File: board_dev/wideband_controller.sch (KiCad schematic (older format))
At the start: 55 parts, among them J1 Conn_02x05_Odd_Even, J2 Conn_01x06, J3 Conn_01x08, Q1 BTS3028, U1 MCP6004, U2 MCP6004, U4 STM32F042K6Ux, U9 XC6206P332MR

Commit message: cleanup & tweaks
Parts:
- R1: value 15k -> 10k; LCSC (none) -> C25744
- R5, R7: value 30k -> 27k; LCSC (none) -> C25711
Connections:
- net +3V3: now also U1.4 (V+); no longer U1.11 (V-)
- net GND: now also U1.11 (V-); no longer U1.4 (V+)
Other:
- note added: "Un_sense = 2.7 * (Un - Vm)"
- note removed: "Un_sense = 3 * (Un - Vm)"
- moved on the sheet: C10, C11, C12, C13, C14, C15, C7, C8, C9, D1, D2, J1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

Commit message: add note
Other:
- note added: "0.2v reference"
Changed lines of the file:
@@
 	1    0    0    -1
 $EndComp
+Text Notes 1175 5150 0    50   ~ 0
+0.2v reference
 $EndSCHEMATC

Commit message: layout help from dave
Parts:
- added C16: 1u, Capacitor_SMD:C_0402_1005Metric, symbol Device:C
- C6: value 3.3n -> 1n; LCSC C26404 -> C1523
- R16: value 10k -> 3.3k; LCSC C25744 -> C25890
- R6: value 20k -> 22k; LCSC (none) -> C25768
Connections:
- net +3V3: now also C16.1
- net GND: now also C16.2
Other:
- note removed: "0.2v reference"
- moved on the sheet: C14
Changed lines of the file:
@@
 P 4975 5250
 F 0 "R6" V 4768 5250 50  0000 C CNN
-F 1 "20k" V 4859 5250 50  0000 C CNN
+F 1 "22k" V 4859 5250 50  0000 C CNN
 F 2 "Resistor_SMD:R_0402_1005Metric" V 4905 5250 50  0001 C CNN
 F 3 "~" H 4975 5250 50  0001 C CNN
+F 4 "C25768" H 4975 5250 50  0001 C CNN "LCSC"
 	1    4975 5250
 	-1   0    0    1
@@
 P 2400 5700
 F 0 "C6" V 2350 5550 50  0000 C CNN
-F 1 "3.3n" V 2350 5850 50  0000 C CNN
+F 1 "1n" V 2350 5850 50  0000 C CNN
 F 2 "Capacitor_SMD:C_0402_1005Metric" H 2438 5550 50  0001 C CNN
 F 3 "~" H 2400 5700 50  0001 C CNN
-F 4 "C26404" H 2400 5700 50  0001 C CNN "LCSC"
+F 4 "C1523" H 2400 5700 50  0001 C CNN "LCSC"
 	1    2400 5700
 	0    1    1    0
@@
 P 2100 5975
 F 0 "R16" V 2000 5975 50  0000 C CNN
-F 1 "10k" V 2100 5975 50  0000 C CNN
+F 1 "3.3k" V 2100 5975 50  0000 C CNN
 F 2 "Resistor_SMD:R_0402_1005Metric" V 2030 5975 50  0001 C CNN
 F 3 "~" H 2100 5975 50  0001 C CNN
-F 4 "C25744" H 2100 5975 50  0001 C CNN "LCSC"
+F 4 "C25890" H 2100 5975 50  0001 C CNN "LCSC"
 	1    2100 5975
 	-1   0    0    1
@@
 	2875 5375 2875 5275
 Connection ~ 2875 5275
-$Comp
-L Amplifier_Operational:MCP6004 U2
-U 3 1 5F6C4F7C
-P 2500 5275
-F 0 "U2" H 2500 5642 50  0000 C CNN
-F 1 "MCP6004" H 2500 5551 50  0000 C CNN
-F 2 "Package_SO:TSSOP-14_4.4x5mm_P0.65mm" H 2450 5375 50  0001 C CNN
-F 3 "http://ww1.microchip.com/downloads/en/DeviceDoc/21733j.pdf" H 2550 5475 50  0001 C CNN
-F 4 "C50282" H 2500 5275 50  0001 C CNN "LCSC"
-	3    2500 5275
-	1    0    0    -1
-$EndComp
-$Comp
-L Amplifier_Operational:MCP6004 U2
-U 2 1 5F6C70E6
-P 2500 6250
-F 0 "U2" H 2500 6617 50  0000 C CNN
-F 1 "MCP6004" H 2500 6526 50  0000 C CNN
-F 2 "Package_SO:TSSOP-14_4.4x5mm_P0.65mm" H 2450 6350 50  0001 C CNN
-F 3 "http://ww1.microchip.com/downloads/en/DeviceDoc/21733j.pdf" H 2550 6450 50  0001 C CNN
-F 4 "C50282" H 2500 6250 50  0001 C CNN "LCSC"
-	2    2500 6250
-	-1   0    0    -1
-$EndComp
-$Comp
-L Amplifier_Operational:MCP6004 U2
-U 4 1 5F6C8103
-P 4525 6625
-F 0 "U2" H 4675 6875 50  0000 C CNN
-F 1 "MCP6004" H 4700 6775 50  0000 C CNN
-F 2 "Package_SO:TSSOP-14_4.4x5mm_P0.65mm" H 4475 6725 50  0001 C CNN
-F 3 "http://ww1.microchip.com/downloads/en/DeviceDoc/21733j.pdf" H 4575 6825 50  0001 C CNN
-F 4 "C50282" H 4525 6625 50  0001 C CNN "LCSC"
-	4    4525 6625
-	-1   0    0    -1
-$EndComp
 Text Label 3900 6625 2    50   ~ 0
 LSU_Un_sense
@@
 	3975 6400 3975 7000
 $Comp
-L Amplifier_Operational:MCP6004 U2
-U 5 1 5FBAE53C
-P 775 7200
-F 0 "U2" H 675 7200 50  0000 C CNN
-F 1 "MCP6004" H 950 7350 50  0001 C CNN
-F 2 "Package_SO:TSSOP-14_4.4x5mm_P0.65mm" H 725 7300 50  0001 C CNN
-F 3 "http://ww1.microchip.com/downloads/en/DeviceDoc/21733j.pdf" H 825 7400 50  0001 C CNN
-F 4 "C50282" H 775 7200 50  0001 C CNN "LCSC"
-	5    775  7200
-	1    0    0    -1
-$EndComp
-$Comp
 L Amplifier_Operational:MCP6004 U1
 U 5 1 5FBAFE30
@@
 L Device:C C14
 U 1 1 602BC665
-P 7450 1050
-F 0 "C14" H 7565 1096 50  0000 L CNN
-F 1 "1u" H 7565 1005 50  0000 L CNN
-F 2 "Capacitor_SMD:C_0402_1005Metric" H 7488 900 50  0001 C CNN
-F 3 "~" H 7450 1050 50  0001 C CNN
-F 4 "C52923" H 7450 1050 50  0001 C CNN "LCSC"
-	1    7450 1050
+P 1900 7225
+F 0 "C14" H 2015 7271 50  0000 L CNN
+F 1 "1u" H 2015 7180 50  0000 L CNN
+F 2 "Capacitor_SMD:C_0402_1005Metric" H 1938 7075 50  0001 C CNN
+F 3 "~" H 1900 7225 50  0001 C CNN
+F 4 "C52923" H 1900 7225 50  0001 C CNN "LCSC"
+	1    1900 7225
 	1    0    0    -1
 $EndComp
@@
 L power:+3.3V #PWR0116
 U 1 1 602BD44D
-P 7450 900
-F 0 "#PWR0116" H 7450 750 50  0001 C CNN
-F 1 "+3.3V" H 7465 1073 50  0000 C CNN
-F 2 "" H 7450 900 50  0001 C CNN
-F 3 "" H 7450 900 50  0001 C CNN
-	1    7450 900
+P 1900 7075
+F 0 "#PWR0116" H 1900 6925 50  0001 C CNN
+F 1 "+3.3V" H 1915 7248 50  0000 C CNN
+F 2 "" H 1900 7075 50  0001 C CNN
+F 3 "" H 1900 7075 50  0001 C CNN
+	1    1900 7075
 	1    0    0    -1
 $EndComp
@@
 L power:GND #PWR0117
 U 1 1 602BD8DF
-P 7450 1200
-F 0 "#PWR0117" H 7450 950 50  0001 C CNN
-F 1 "GND" H 7455 1027 50  0000 C CNN
-F 2 "" H 7450 1200 50  0001 C CNN
-F 3 "" H 7450 1200 50  0001 C CNN
-	1    7450 1200
+P 1900 7375
+F 0 "#PWR0117" H 1900 7125 50  0001 C CNN
+F 1 "GND" H 1905 7202 50  0000 C CNN
+F 2 "" H 1900 7375 50  0001 C CNN
+F 3 "" H 1900 7375 50  0001 C CNN
+	1    1900 7375
 	1    0    0    -1
 $EndComp
@@
 	1    0    0    -1
 $EndComp
-Text Notes 1175 5150 0    50   ~ 0
-0.2v reference
+$Comp
+L Amplifier_Operational:MCP6004 U2
+U 2 1 5F6C70E6
+P 2500 6250
+F 0 "U2" H 2500 6617 50  0000 C CNN
+F 1 "MCP6004" H 2500 6526 50  0000 C CNN
+F 2 "Package_SO:TSSOP-14_4.4x5mm_P0.65mm" H 2450 6350 50  0001 C CNN
+F 3 "http://ww1.microchip.com/downloads/en/DeviceDoc/21733j.pdf" H 2550 6450 50  0001 C CNN
+F 4 "C50282" H 2500 6250 50  0001 C CNN "LCSC"
+	2    2500 6250
+	-1   0    0    -1
+$EndComp
+$Comp
+L Amplifier_Operational:MCP6004 U2
+U 4 1 5F6C8103
+P 4525 6625
+F 0 "U2" H 4675 6875 50  0000 C CNN
+F 1 "MCP6004" H 4700 6775 50  0000 C CNN
+F 2 "Package_SO:TSSOP-14_4.4x5mm_P0.65mm" H 4475 6725 50  0001 C CNN
+F 3 "http://ww1.microchip.com/downloads/en/DeviceDoc/21733j.pdf" H 4575 6825 50  0001 C CNN
+F 4 "C50282" H 4525 6625 50  0001 C CNN "LCSC"
+	4    4525 6625
+	-1   0    0    -1
+$EndComp
+$Comp
+L Amplifier_Operational:MCP6004 U2
+U 5 1 5FBAE53C
+P 775 7200
+F 0 "U2" H 675 7200 50  0000 C CNN
+F 1 "MCP6004" H 950 7350 50  0001 C CNN
+F 2 "Package_SO:TSSOP-14_4.4x5mm_P0.65mm" H 725 7300 50  0001 C CNN
+F 3 "http://ww1.microchip.com/downloads/en/DeviceDoc/21733j.pdf" H 825 7400 50  0001 C CNN
+F 4 "C50282" H 775 7200 50  0001 C CNN "LCSC"
+	5    775  7200
+	1    0    0    -1
+$EndComp
+$Comp
+L Amplifier_Operational:MCP6004 U2
+U 3 1 5F6C4F7C
+P 2500 5275
+F 0 "U2" H 2500 5642 50  0000 C CNN
+F 1 "MCP6004" H 2500 5551 50  0000 C CNN
+F 2 "Package_SO:TSSOP-14_4.4x5mm_P0.65mm" H 2450 5375 50  0001 C CNN
+F 3 "http://ww1.microchip.com/downloads/en/DeviceDoc/21733j.pdf" H 2550 5475 50  0001 C CNN
+F 4 "C50282" H 2500 5275 50  0001 C CNN "LCSC"
+	3    2500 5275
+	1    0    0    -1
+$EndComp
+$Comp
+L Device:C C16
+U 1 1 5F67CE20
+P 1450 7225
+F 0 "C16" H 1565 7271 50  0000 L CNN
+F 1 "1u" H 1565 7180 50  0000 L CNN
+F 2 "Capacitor_SMD:C_0402_1005Metric" H 1488 7075 50  0001 C CNN
+F 3 "~" H 1450 7225 50  0001 C CNN
+F 4 "C52923" H 1450 7225 50  0001 C CNN "LCSC"
+	1    1450 7225
+	1    0    0    -1
+$EndComp
+$Comp
+L power:+3.3V #PWR0123
+U 1 1 5F67CE26
+P 1450 7075
+F 0 "#PWR0123" H 1450 6925 50  0001 C CNN
+F 1 "+3.3V" H 1465 7248 50  0000 C CNN
+F 2 "" H 1450 7075 50  0001 C CNN
+F 3 "" H 1450 7075 50  0001 C CNN
+	1    1450 7075
+	1    0    0    -1
+$EndComp
+$Comp
+L power:GND #PWR0124
+U 1 1 5F67CE2C
+P 1450 7375
+F 0 "#PWR0124" H 1450 7125 50  0001 C CNN
+F 1 "GND" H 1455 7202 50  0000 C CNN
+F 2 "" H 1450 7375 50  0001 C CNN
+F 3 "" H 1450 7375 50  0001 C CNN
+	1    1450 7375
+	1    0    0    -1
+$EndComp
 $EndSCHEMATC

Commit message: pcb tweakery
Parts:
- removed C15: 100n, Capacitor_SMD:C_0402_1005Metric, symbol Device:C
- removed R28: 3.3k, Resistor_SMD:R_0402_1005Metric, symbol Device:R
- added R31, R32: 68k, Resistor_SMD:R_0402_1005Metric, symbol Device:R
- added R33, R34: 10k, Resistor_SMD:R_0402_1005Metric, symbol Device:R
- C3: value 100n -> 33n; LCSC C1525 -> C1585
- R8: value 10 -> 47; LCSC C25077 -> C25118
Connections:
- net GND: no longer C3.2
- net Ip_dac: now also U4.12 (PA6), R31.1; no longer U1.3 (+)
- net Ip_sense: now also C11.1, R24.2, U4.8 (PA2); no longer R17.1, R24.1, U1.8
- net LSU_Rtrim: now also R34.1; no longer C3.1
- net Vm: now also R32.2
- net at R8.2, U1.1: now also C3.1, R33.1; no longer U1.2 (-)
- new net: R17.1, R24.1, U1.8
- new net: C3.2, R31.2, R33.2, U1.2 (-)
- new net: R32.1, R34.2, U1.3 (+)
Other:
- moved on the sheet: C11, R10, R11, R12, R15, R17, R24, R8, U1A, U1C

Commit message: fix jlc numbers
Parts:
- R15, R17: LCSC C25471 -> C25741
- R23: LCSC C23140 -> C25105
- R5, R7: LCSC C25711 -> C25771
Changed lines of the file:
@@
 F 2 "Resistor_SMD:R_0402_1005Metric" V 3705 3875 50  0001 C CNN
 F 3 "~" H 3775 3875 50  0001 C CNN
-F 4 "C25471" H 3775 3875 50  0001 C CNN "LCSC"
+F 4 "C25741" H 3775 3875 50  0001 C CNN "LCSC"
 	1    3775 3875
 	0    1    1    0
@@
 F 2 "Resistor_SMD:R_0402_1005Metric" V 4280 3075 50  0001 C CNN
 F 3 "~" H 4350 3075 50  0001 C CNN
-F 4 "C25471" H 4350 3075 50  0001 C CNN "LCSC"
+F 4 "C25741" H 4350 3075 50  0001 C CNN "LCSC"
 	1    4350 3075
 	0    1    1    0
@@
 F 2 "Resistor_SMD:R_0402_1005Metric" V 4880 825 50  0001 C CNN
 F 3 "~" H 4950 825 50  0001 C CNN
-F 4 "C25711" H 4950 825 50  0001 C CNN "LCSC"
+F 4 "C25771" H 4950 825 50  0001 C CNN "LCSC"
 	1    4950 825
 	0    -1   -1   0
@@
 F 2 "Resistor_SMD:R_0402_1005Metric" V 4230 1550 50  0001 C CNN
 F 3 "~" H 4300 1550 50  0001 C CNN
-F 4 "C25711" H 4300 1550 50  0001 C CNN "LCSC"
+F 4 "C25771" H 4300 1550 50  0001 C CNN "LCSC"
 	1    4300 1550
 	0    1    1    0
@@
 F 2 "Resistor_SMD:R_0402_1005Metric" V 7605 1900 50  0001 C CNN
 F 3 "~" H 7675 1900 50  0001 C CNN
-F 4 "C23140" H 7675 1900 50  0001 C CNN "LCSC"
+F 4 "C25105" H 7675 1900 50  0001 C CNN "LCSC"
 	1    7675 1900
 	1    0    0    -1

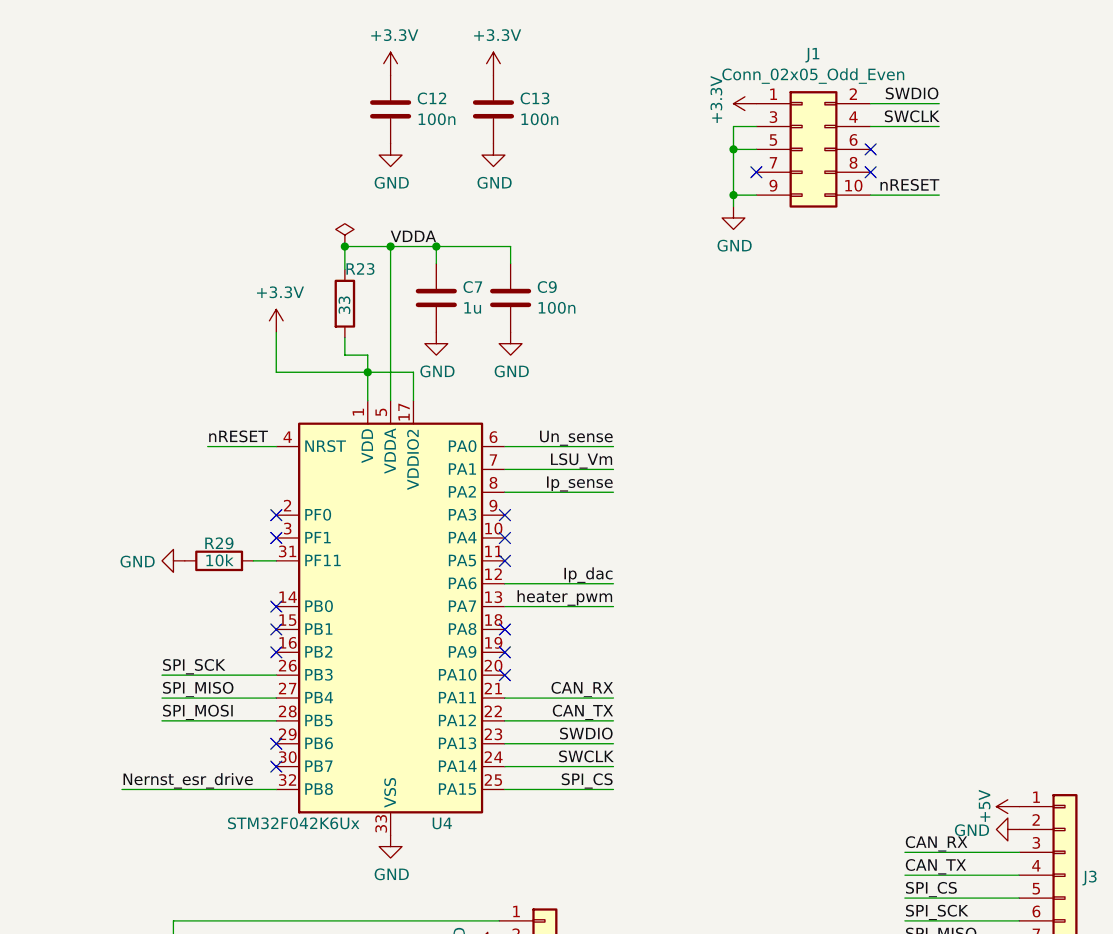
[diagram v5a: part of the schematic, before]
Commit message: switch to 14 pin stlinkv3 connector
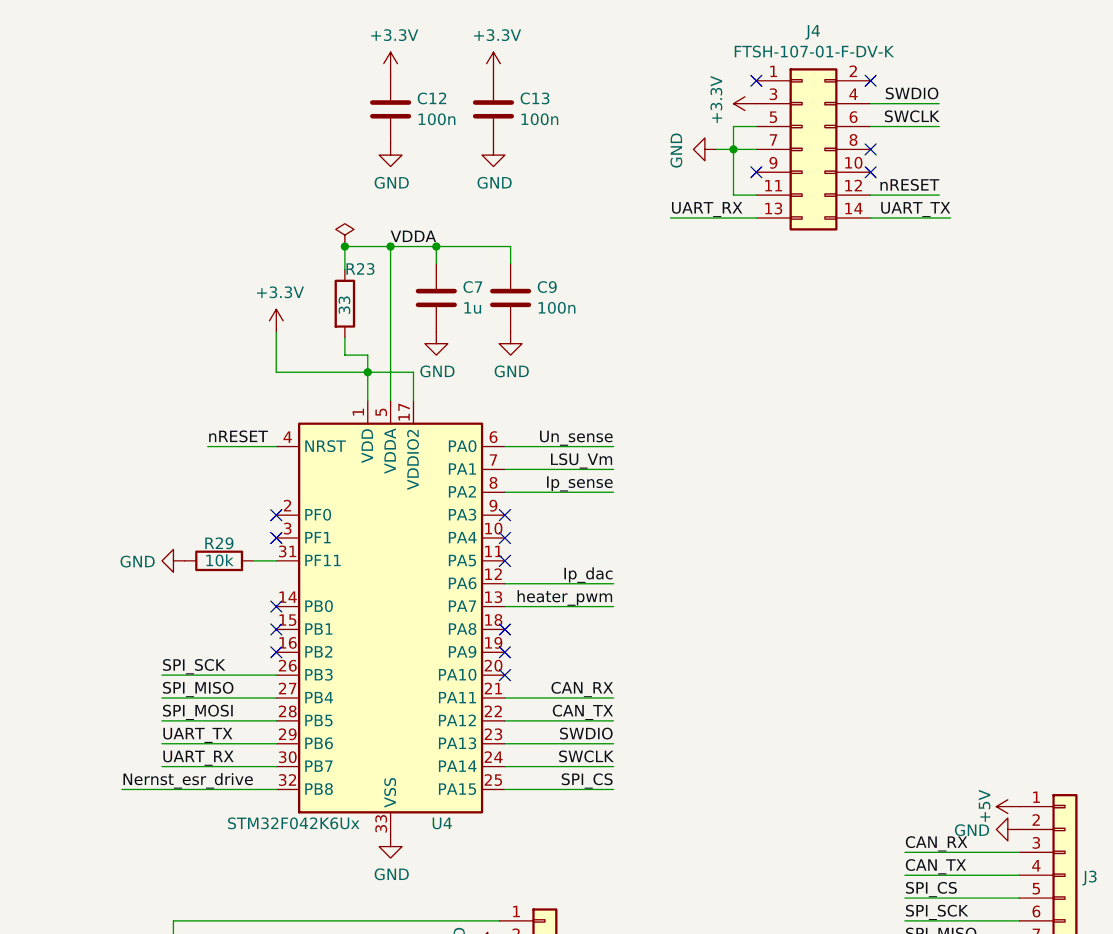
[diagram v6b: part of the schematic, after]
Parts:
- removed J1: Conn_02x05_Odd_Even, Connector_PinHeader_1.27mm:PinHeader_2x05_P1.27mm_Vertical_SMD, symbol Connector_Generic:Conn_02x05_Odd_Even
- added J4: FTSH-107-01-F-DV-K, Connector_PinHeader_1.27mm:PinHeader_2x07_P1.27mm_Vertical_SMD, symbol Connector_Generic:Conn_02x07_Odd_Even
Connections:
- net +3V3: now also J4.3 (Pin_3)
- net GND: now also J4.11 (Pin_11), J4.5 (Pin_5), J4.7 (Pin_7)
- net SWCLK: now also J4.6 (Pin_6)
- net SWDIO: now also J4.4 (Pin_4)
- net nRESET: now also J4.12 (Pin_12)
- net UART_TX: now reaches U4.29 (PB6)
- net UART_TX: now also J4.14 (Pin_14)
- net UART_RX: now reaches U4.30 (PB7)
- net UART_RX: now also J4.13 (Pin_13)
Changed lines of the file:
@@
-$EndComp
-$Comp
-L Connector_Generic:Conn_02x05_Odd_Even J1
-U 1 1 5ECAA616
-P 9675 1225
-F 0 "J1" H 9725 1642 50  0000 C CNN
-F 1 "Conn_02x05_Odd_Even" H 9725 1551 50  0000 C CNN
-F 2 "Connector_PinHeader_1.27mm:PinHeader_2x05_P1.27mm_Vertical_SMD" H 9675 1225 50  0001 C CNN
-F 3 "~" H 9675 1225 50  0001 C CNN
-	1    9675 1225
-	1    0    0    -1
 $EndComp
 $Comp
@@
 L power:GND #PWR017
 U 1 1 5ECABF9C
-P 9375 1475
-F 0 "#PWR017" H 9375 1225 50  0001 C CNN
-F 1 "GND" H 9380 1302 50  0000 C CNN
-F 2 "" H 9375 1475 50  0001 C CNN
-F 3 "" H 9375 1475 50  0001 C CNN
-	1    9375 1475
-	1    0    0    -1
-$EndComp
-Wire Wire Line
-	9375 1475 9375 1425
+P 9300 1225
+F 0 "#PWR017" H 9300 975 50  0001 C CNN
+F 1 "GND" H 9305 1052 50  0000 C CNN
+F 2 "" H 9300 1225 50  0001 C CNN
+F 3 "" H 9300 1225 50  0001 C CNN
+	1    9300 1225
+	0    1    1    0
+$EndComp
 Wire Wire Line
 	9375 1125 9475 1125
@@
 Wire Wire Line
 	9475 1425 9375 1425
-Connection ~ 9375 1425
 Wire Wire Line
 	9375 1425 9375 1225
@@
 NoConn ~ 7375 2925
 NoConn ~ 7375 2825
-NoConn ~ 7375 3825
-NoConn ~ 7375 3925
 $Comp
 L power:GND #PWR0120
@@
 NoConn ~ 8375 3025
 NoConn ~ 8375 3325
-NoConn ~ 8375 3425
-NoConn ~ 8375 3525
 NoConn ~ 7375 3425
 NoConn ~ 7375 3325
@@
 Wire Wire Line
 	8375 2725 8850 2725
+$Comp
+L Connector_Generic:Conn_02x07_Odd_Even J4
+U 1 1 5FAC09D3
+P 9675 1225
+F 0 "J4" H 9725 1742 50  0000 C CNN
+F 1 "FTSH-107-01-F-DV-K" H 9725 1651 50  0000 C CNN
+F 2 "Connector_PinHeader_1.27mm:PinHeader_2x07_P1.27mm_Vertical_SMD" H 9675 1225 50  0001 C CNN
+F 3 "~" H 9675 1225 50  0001 C CNN
+	1    9675 1225
+	1    0    0    -1
+$EndComp
+NoConn ~ 9975 925
+NoConn ~ 9475 925
+Text Label 9100 1525 0    50   ~ 0
+UART_RX
+Text Label 10325 1525 2    50   ~ 0
+UART_TX
+Wire Wire Line
+	9975 1525 10325 1525
+Wire Wire Line
+	9300 1225 9375 1225
+Wire Wire Line
+	9100 1525 9475 1525
+Text Label 6875 3925 0    50   ~ 0
+UART_RX
+Text Label 6875 3825 0    50   ~ 0
+UART_TX
+Wire Wire Line
+	6875 3825 7375 3825
+Wire Wire Line
+	7375 3925 6875 3925
+NoConn ~ 8375 3425
+NoConn ~ 8375 3525
 $EndSCHEMATC
